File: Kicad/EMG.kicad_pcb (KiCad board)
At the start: 2 copper layers, 32 x 38.9 mm, 46 parts, among them IC1 MAX8881EUT33-T, P1 nRF24l01, P2 CONN_01X02, P3 MICRO_USB_B, P4 CONN_01X05, P5 CONN_01X03, SW1 SWITCH_INV, U1 MSP430G2231IPW14, U2 TLC2274, U3 TLC2274, U4 MCP73831

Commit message: Se agregaron los 3d shapes de el cargador y dc/dc
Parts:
- U1, U2, U3: footprint EMG:TSSOP-14_4.4x5mm_Pitch0.65mm -> EMG:TSSOP-14

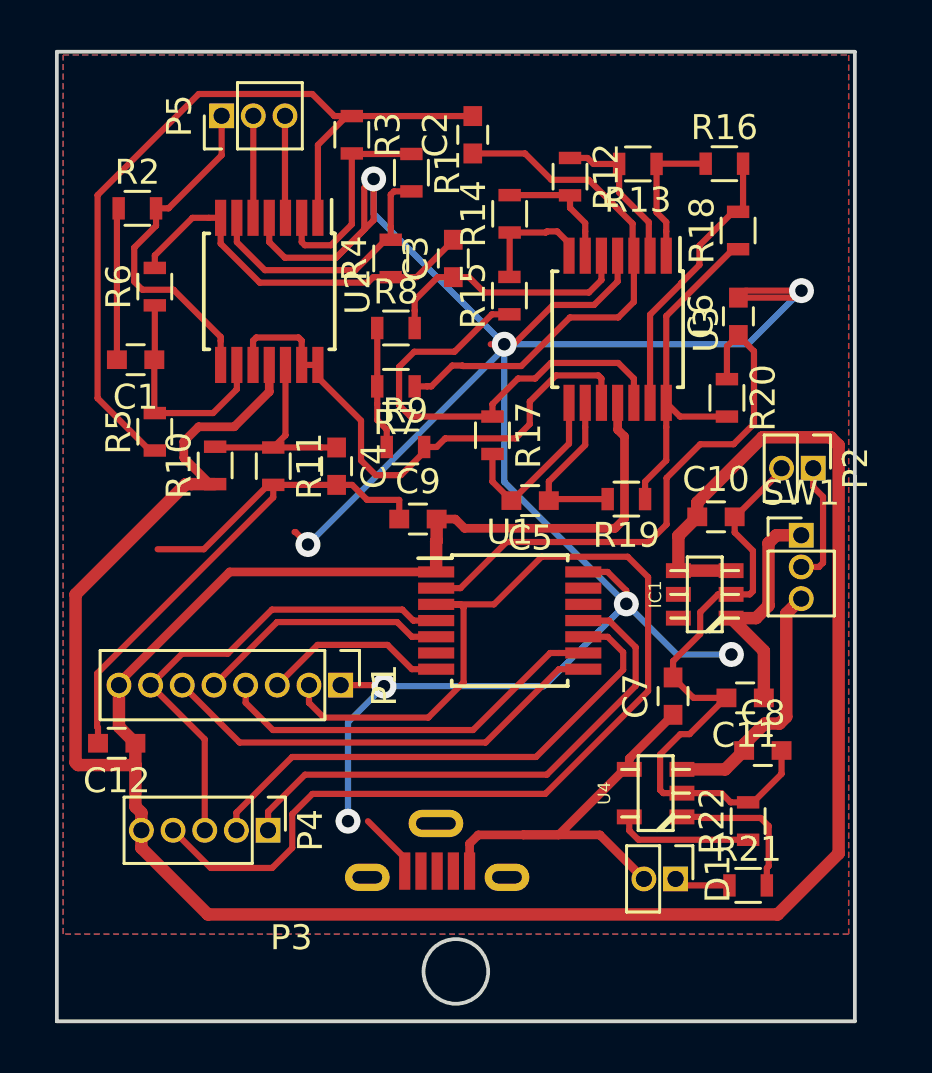
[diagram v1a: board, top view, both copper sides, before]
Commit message: Cambiado el tamaño de las vías de conexión a tierra para que coincida con el de los pin headers (un solo taladro)
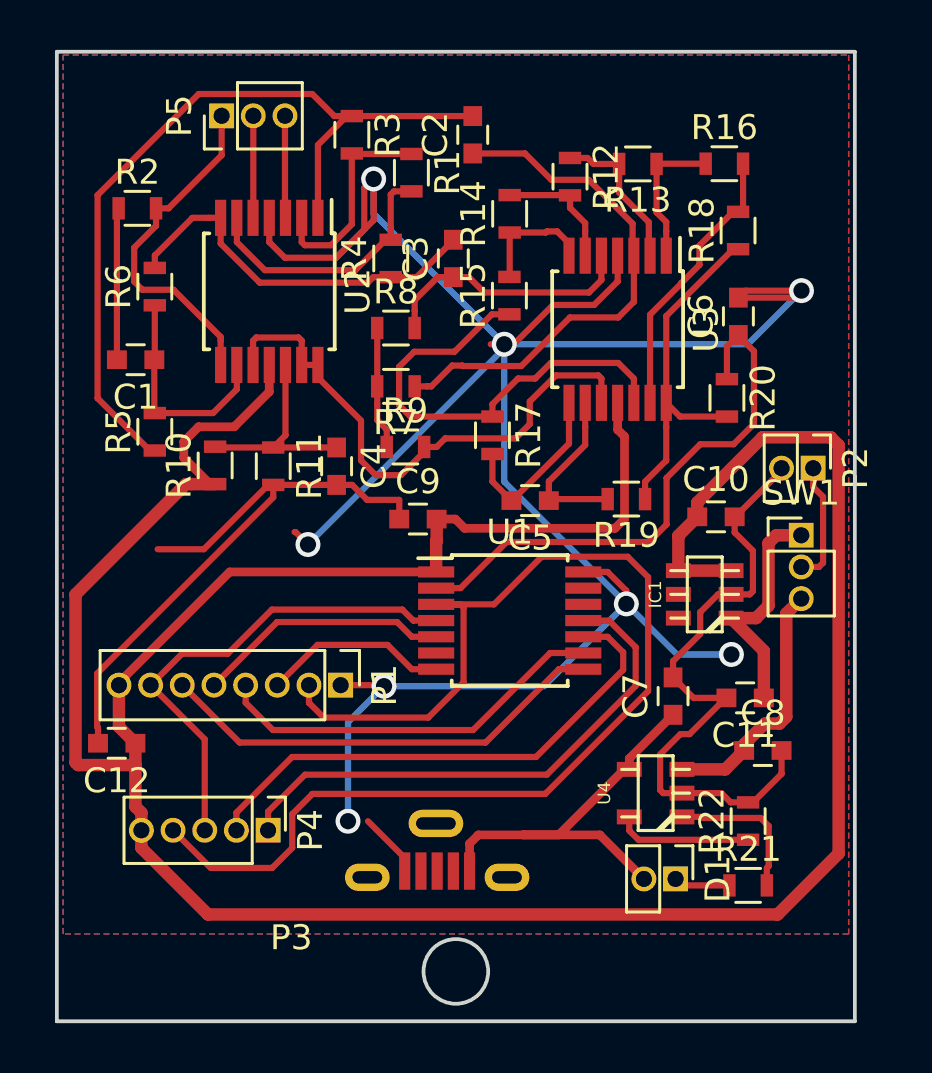
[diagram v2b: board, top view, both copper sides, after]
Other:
- net class Mayer10mils: via_drill 0.5 -> 0.65
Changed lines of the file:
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@@
-(kicad_pcb (version 4) (host pcbnew 4.0.4-stable)
+(kicad_pcb (version 4) (host pcbnew 4.0.2-stable)
   (general
     (links 100)
@@
     (mod_text_size 1 1)
     (mod_text_width 0.15)
-    (pad_size 0.4 1.5)
-    (pad_drill 0)
+    (pad_size 1 1)
+    (pad_drill 0.65)
     (pad_to_mask_clearance 0.2)
     (aux_axis_origin 0 0)
     (visible_elements 7FFEFFFF)
     (pcbplotparams
-      (layerselection 0x00030_80000001)
+      (layerselection 0x01030_80000001)
       (usegerberextensions false)
       (excludeedgelayer true)
@@
       (outputformat 1)
       (mirror false)
-      (drillshape 1)
+      (drillshape 0)
       (scaleselection 1)
       (outputdirectory ""))
@@
     (uvia_dia 0.3)
     (uvia_drill 0.1)
-    (add_net "Net-(P3-Pad4)")
-    (add_net VDD)
   )
   (net_class Mayer10mils ""
@@
     (trace_width 0.25)
     (via_dia 1)
-    (via_drill 0.5)
+    (via_drill 0.65)
     (uvia_dia 0.3)
     (uvia_drill 0.1)
@@
     (add_net "Net-(P3-Pad2)")
     (add_net "Net-(P3-Pad3)")
+    (add_net "Net-(P3-Pad4)")
     (add_net "Net-(P5-Pad1)")
     (add_net "Net-(P5-Pad2)")
@@
     (add_net TEST)
     (add_net VCC)
+    (add_net VDD)
   )
   (module EMG:C_0603 (layer F.Cu)
@@
   (segment (start 153.95 151.975) (end 153.95 151.45) (width 0.25) (layer F.Cu) (net 8))
   (segment (start 153.95 151.45) (end 152.475 149.975) (width 0.25) (layer F.Cu) (net 8))
-  (via (at 151.675 149.975) (size 1) (drill 0.5) (layers F.Cu B.Cu) (net 8))
+  (via (at 151.675 149.975) (size 1) (drill 0.65) (layers F.Cu B.Cu) (net 8))
   (segment (start 167.33 128.98) (end 169.58 128.98) (width 0.25) (layer F.Cu) (net 8))
   (segment (start 169.58 128.98) (end 169.86 128.7) (width 0.25) (layer F.Cu) (net 8))
@@
   (segment (start 167.205 137.77) (end 169.06 135.915) (width 0.25) (layer F.Cu) (net 8))
   (segment (start 169.06 135.915) (end 169.06 135.82) (width 0.25) (layer F.Cu) (net 8))
-  (via (at 150.07 138.88) (size 1) (drill 0.5) (layers F.Cu B.Cu) (net 8))
-  (via (at 169.86 128.7) (size 1) (drill 0.5) (layers F.Cu B.Cu) (net 8))
+  (via (at 150.07 138.88) (size 1) (drill 0.65) (layers F.Cu B.Cu) (net 8))
+  (via (at 169.86 128.7) (size 1) (drill 0.65) (layers F.Cu B.Cu) (net 8))
   (segment (start 157.94 130.849231) (end 157.397709 130.849231) (width 0.25) (layer F.Cu) (net 8))
   (segment (start 162.487709 127.299231) (end 162.487709 128.331359) (width 0.25) (layer F.Cu) (net 8))
@@
   (segment (start 159.8977 129.274242) (end 158.322711 130.849231) (width 0.25) (layer F.Cu) (net 8))
   (segment (start 158.322711 130.849231) (end 157.94 130.849231) (width 0.25) (layer F.Cu) (net 8))
-  (via (at 157.94 130.849231) (size 1) (drill 0.5) (layers F.Cu B.Cu) (net 8))
+  (via (at 157.94 130.849231) (size 1) (drill 0.65) (layers F.Cu B.Cu) (net 8))
   (segment (start 151.19982 127.379242) (end 152.702719 125.876343) (width 0.25) (layer F.Cu) (net 8))
   (segment (start 152.702719 125.876343) (end 152.702719 124.22195) (width 0.25) (layer F.Cu) (net 8))
-  (via (at 152.702719 124.22195) (size 1) (drill 0.5) (layers F.Cu B.Cu) (net 8))
+  (via (at 152.702719 124.22195) (size 1) (drill 0.65) (layers F.Cu B.Cu) (net 8))
   (segment (start 148.677709 136.489231) (end 148.477709 136.489231) (width 0.25) (layer F.Cu) (net 8))
   (segment (start 148.477709 136.489231) (end 145.89694 139.07) (width 0.25) (layer F.Cu) (net 8))
@@
   (segment (start 151.38 144.52) (end 153.08 144.52) (width 0.25) (layer F.Cu) (net 8))
   (segment (start 153.08 144.52) (end 153.12 144.56) (width 0.25) (layer F.Cu) (net 8))
-  (via (at 153.12 144.56) (size 1) (drill 0.5) (layers F.Cu B.Cu) (net 8))
-  (via (at 167.05 143.29) (size 1) (drill 0.5) (layers F.Cu B.Cu) (net 8))
+  (via (at 153.12 144.56) (size 1) (drill 0.65) (layers F.Cu B.Cu) (net 8))
+  (via (at 167.05 143.29) (size 1) (drill 0.65) (layers F.Cu B.Cu) (net 8))
   (segment (start 161.11 139.98) (end 162.085 139.98) (width 0.25) (layer F.Cu) (net 8))
   (segment (start 162.085 139.98) (end 162.83501 140.73001) (width 0.25) (layer F.Cu) (net 8))
   (segment (start 162.83501 140.73001) (end 162.83501 141.26) (width 0.25) (layer F.Cu) (net 8))
-  (via (at 162.83501 141.26) (size 1) (drill 0.5) (layers F.Cu B.Cu) (net 8))
+  (via (at 162.83501 141.26) (size 1) (drill 0.65) (layers F.Cu B.Cu) (net 8))
   (segment (start 148.677709 136.489231) (end 148.677709 136.989231) (width 0.25) (layer F.Cu) (net 8))
   (segment (start 148.677709 136.989231) (end 141.614999 144.051941) (width 0.25) (layer F.Cu) (net 8))

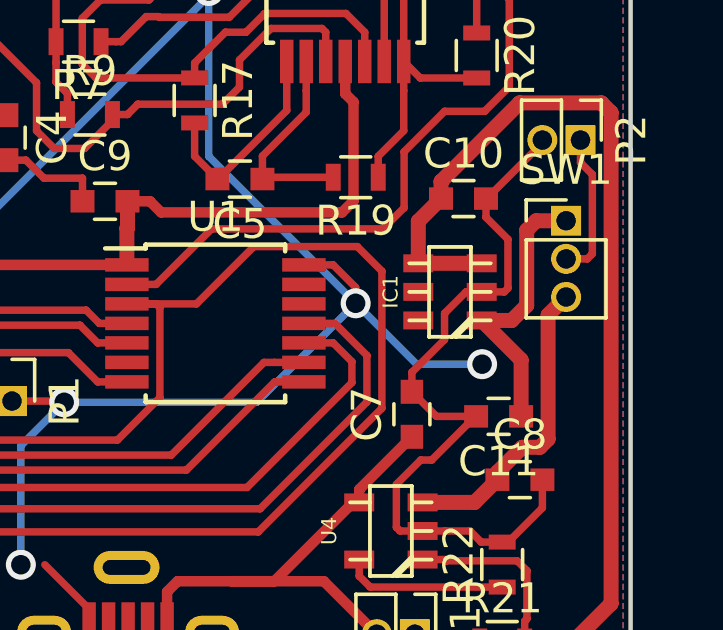
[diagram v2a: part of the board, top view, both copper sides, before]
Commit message: Conexión de /SHDN a IN del DC/DC
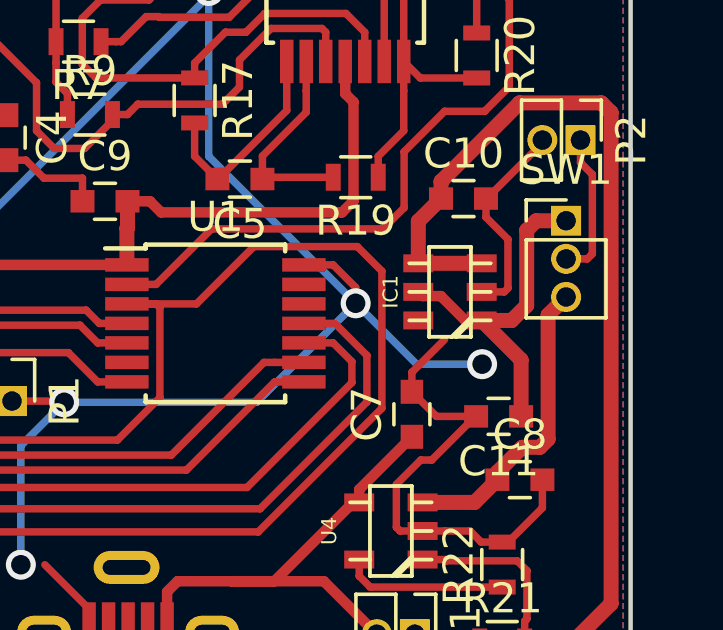
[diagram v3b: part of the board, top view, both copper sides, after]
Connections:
- IC1 pad 5: Net-(IC1-Pad5) -> +BATT
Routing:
- net +BATT: track 9.43 -> 11.9 mm
- net GND: track 149.3 -> 146.9 mm

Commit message: Modificado modelo 3D del USB para que coincida con la placa.
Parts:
- C10: value C -> 4,7uF
- C11: value C -> 1uF
- C7, C8: value CP -> 4,7uF
- R21: value R -> 470
- R22: value R -> 2K
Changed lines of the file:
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@@
   (general
     (links 101)
-    (no_connects 1)
+    (no_connects 0)
     (area 139.924999 119.044999 172.075001 158.075001)
     (thickness 1.6)
@@
       (effects (font (size 1 1) (thickness 0.15)))
     )
-    (fp_text value CP (at 0 1.5 90) (layer F.Fab)
+    (fp_text value 4,7uF (at 0 1.5 90) (layer F.Fab)
       (effects (font (size 1 1) (thickness 0.15)))
     )
@@
       (effects (font (size 1 1) (thickness 0.15)))
     )
-    (fp_text value CP (at 0 1.5) (layer F.Fab)
+    (fp_text value 4,7uF (at 0 1.5) (layer F.Fab)
       (effects (font (size 1 1) (thickness 0.15)))
     )
@@
       (effects (font (size 1 1) (thickness 0.15)))
     )
-    (fp_text value C (at 0 1.5) (layer F.Fab)
+    (fp_text value 4,7uF (at 0 1.5) (layer F.Fab)
       (effects (font (size 1 1) (thickness 0.15)))
     )
@@
       (effects (font (size 1 1) (thickness 0.15)))
     )
-    (fp_text value C (at 0 1.5 180) (layer F.Fab)
+    (fp_text value 1uF (at 0 1.5 180) (layer F.Fab)
       (effects (font (size 1 1) (thickness 0.15)))
     )
@@
       (effects (font (size 1 1) (thickness 0.15)))
     )
-    (fp_text value R (at 0 1.5) (layer F.Fab)
+    (fp_text value 470 (at 0 1.5) (layer F.Fab)
       (effects (font (size 1 1) (thickness 0.15)))
     )
@@
       (effects (font (size 1 1) (thickness 0.15)))
     )
-    (fp_text value R (at 0 1.5 90) (layer F.Fab)
+    (fp_text value 2K (at 0 1.5 90) (layer F.Fab)
       (effects (font (size 1 1) (thickness 0.15)))
     )
@@
       (rotate (xyz 0 0 0))
     )
-  )
-  (module EMG:usb_vert_2 (layer F.Cu)
-    (at 155.25 151.975 180)
-    (fp_text reference P3 (at 5.85 -2.67 180) (layer F.SilkS)
-      (effects (font (size 1 1) (thickness 0.15)))
-    )
-    (fp_text value MICRO_USB_B (at 0.01 -3.59 180) (layer F.Fab) hide
-      (effects (font (size 1 1) (thickness 0.15)))
-    )
-    (pad 3 smd rect (at 0 0 180) (size 0.45 1.5) (layers F.Cu F.Paste F.Mask)
-      (net 24 "Net-(P3-Pad3)"))
-    (pad 4 smd rect (at 0.65 0 180) (size 0.45 1.5) (layers F.Cu F.Paste F.Mask)
-      (net 48 "Net-(P3-Pad4)"))
-    (pad 2 smd rect (at -0.65 0 180) (size 0.45 1.5) (layers F.Cu F.Paste F.Mask)
-      (net 25 "Net-(P3-Pad2)"))
-    (pad 5 smd rect (at 1.3 0 180) (size 0.45 1.5) (layers F.Cu F.Paste F.Mask)
-      (net 8 GND))
-    (pad 1 smd rect (at -1.3 0 180) (size 0.45 1.5) (layers F.Cu F.Paste F.Mask)
-      (net 12 "Net-(C7-Pad1)"))
-    (pad 6 thru_hole oval (at 2.8 -0.25 270) (size 1.1 1.8) (drill oval 0.5 1.2) (layers *.Cu *.Mask))
-    (pad 6 thru_hole oval (at -2.8 -0.25 270) (size 1.1 1.8) (drill oval 0.5 1.2) (layers *.Cu *.Mask))
-    (pad 6 thru_hole oval (at 0.05 1.91 270) (size 1.1 2.2) (drill oval 0.5 1.6) (layers *.Cu *.Mask))
   )
   (module EMG:TSSOP-14 (layer F.Cu)
@@
     )
   )
+  (module EMG:usb_vert_2 (layer F.Cu)
+    (at 155.25 151.975 180)
+    (fp_text reference P3 (at 5.85 -2.67 180) (layer F.SilkS)
+      (effects (font (size 1 1) (thickness 0.15)))
+    )
+    (fp_text value MICRO_USB_B (at 0.01 -3.59 180) (layer F.Fab) hide
+      (effects (font (size 1 1) (thickness 0.15)))
+    )
+    (pad 3 smd rect (at 0 0 180) (size 0.45 1.5) (layers F.Cu F.Paste F.Mask)
+      (net 24 "Net-(P3-Pad3)"))
+    (pad 4 smd rect (at 0.65 0 180) (size 0.45 1.5) (layers F.Cu F.Paste F.Mask)
+      (net 48 "Net-(P3-Pad4)"))
+    (pad 2 smd rect (at -0.65 0 180) (size 0.45 1.5) (layers F.Cu F.Paste F.Mask)
+      (net 25 "Net-(P3-Pad2)"))
+    (pad 5 smd rect (at 1.3 0 180) (size 0.45 1.5) (layers F.Cu F.Paste F.Mask)
+      (net 8 GND))
+    (pad 1 smd rect (at -1.3 0 180) (size 0.45 1.5) (layers F.Cu F.Paste F.Mask)
+      (net 12 "Net-(C7-Pad1)"))
+    (pad 6 thru_hole oval (at 2.8 -0.25 270) (size 1.1 1.8) (drill oval 0.5 1.2) (layers *.Cu *.Mask))
+    (pad 6 thru_hole oval (at -2.8 -0.25 270) (size 1.1 1.8) (drill oval 0.5 1.2) (layers *.Cu *.Mask))
+    (pad 6 thru_hole oval (at 0.05 1.91 270) (size 1.1 2.2) (drill oval 0.5 1.6) (layers *.Cu *.Mask))
+    (model ${KIPRJMOD}/EMG.3Dshapes/USB.wrl
+      (at (xyz 0 0.005 0.105))
+      (scale (xyz 0.4 0.4 0.4))
+      (rotate (xyz 0 180 180))
+    )
+  )

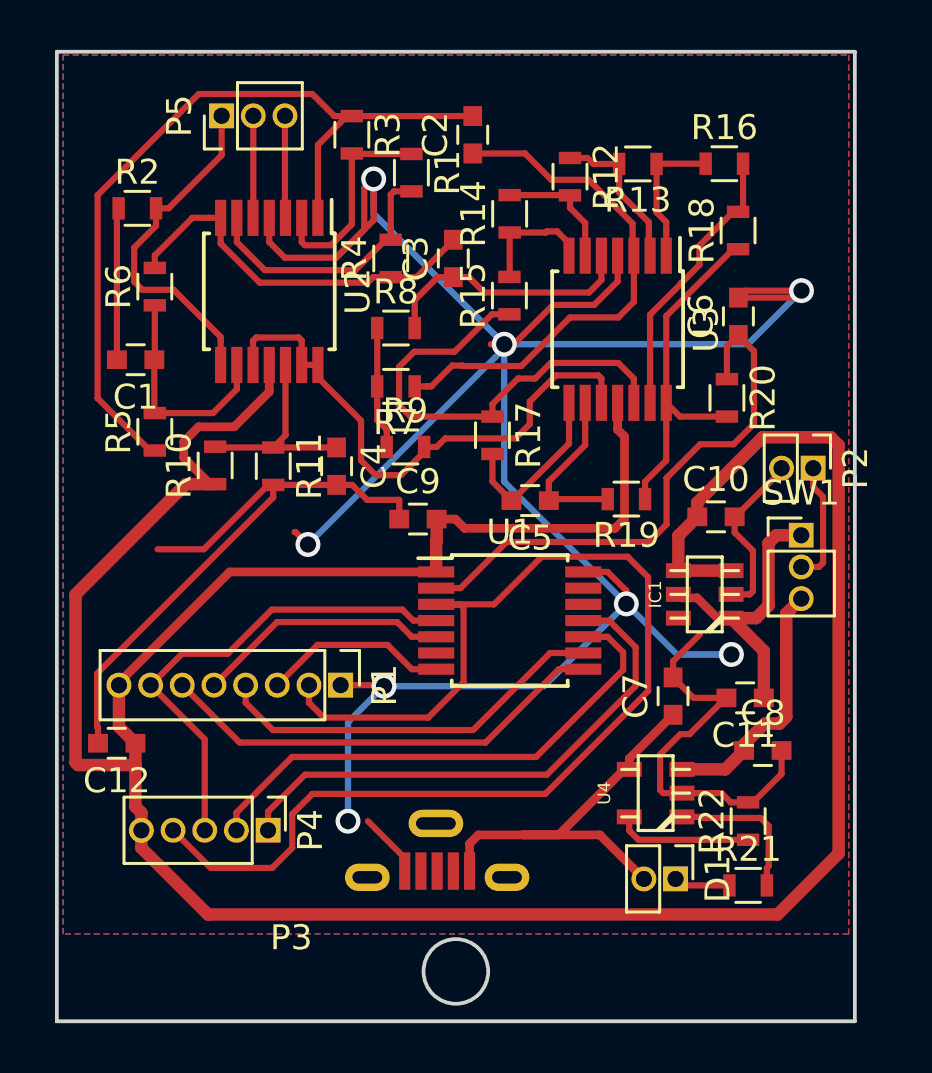
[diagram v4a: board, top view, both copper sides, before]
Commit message: Se cambió el pin out de nRF en el esquemático y se hicieron las nuevas conexiones en el pcb.
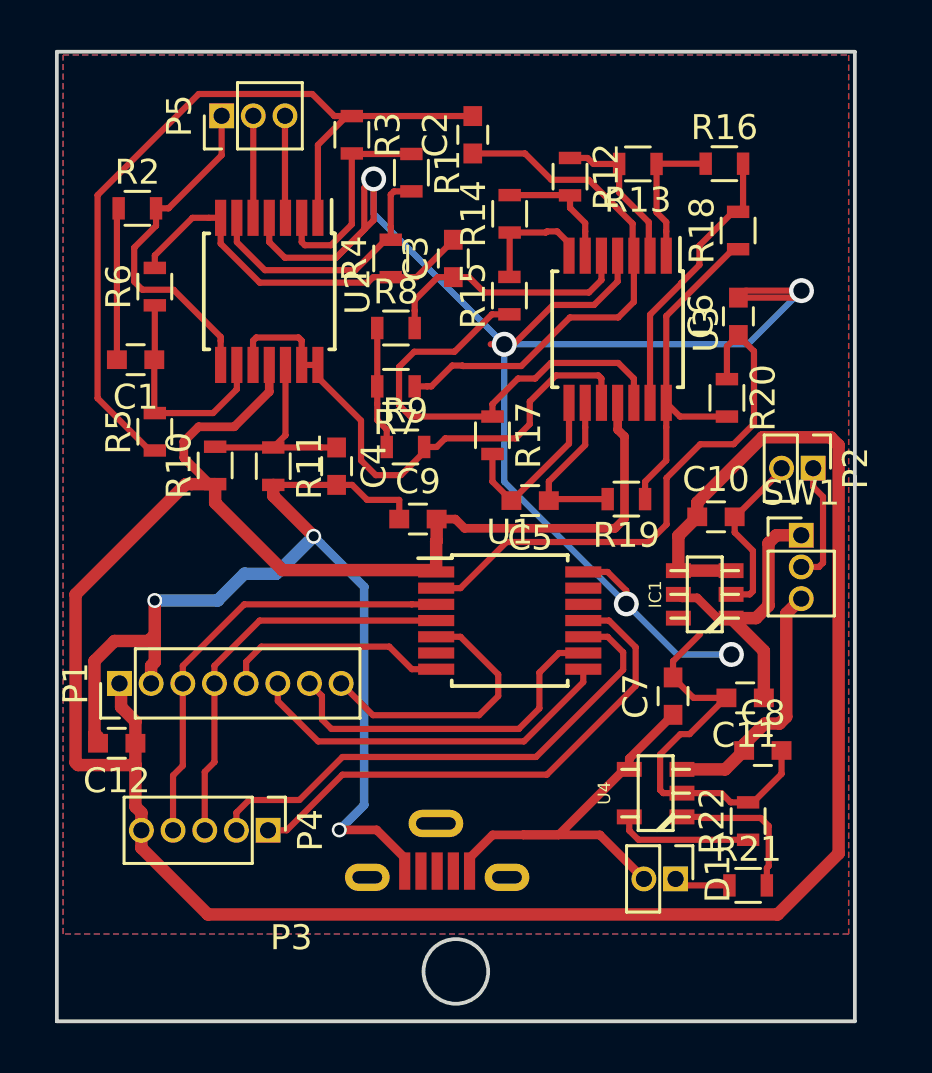
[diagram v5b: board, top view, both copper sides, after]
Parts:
- moved P1 8.87 mm to (142.5, 144.4), turned to 90 degrees
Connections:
- P1 pad 1: GND -> VCC
- P1 pad 2: /Microcontrolador/CE -> GND
- P1 pad 3: /Microcontrolador/SCK -> /Microcontrolador/CE
- P1 pad 4: /Microcontrolador/MISO -> /Microcontrolador/CSN
- P1 pad 5: /Microcontrolador/IRQ -> /Microcontrolador/SCK
- P1 pad 7: /Microcontrolador/CSN -> /Microcontrolador/MISO
- P1 pad 8: VCC -> /Microcontrolador/IRQ
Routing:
- net /Microcontrolador/CE: track 48.7 -> 17.9 mm
- net GND: track 146.9 -> 131.0 mm
- net VCC: track 119.0 -> 115.2 mm
- net /Microcontrolador/CSN: track 19.6 -> 16.4 mm
- net /Microcontrolador/MOSI: track 18.3 -> 15.1 mm
- net /Microcontrolador/SCK: track 7.44 -> 9.11 mm
- net /Microcontrolador/MISO: track 16.0 -> 14.4 mm
- net /Microcontrolador/IRQ: track 10.2 -> 11.1 mm
